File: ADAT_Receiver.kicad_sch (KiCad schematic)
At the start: 21 parts, among them J1 USB_C_Receptacle_PowerOnly_6P, J2 PLR135-T, J3 Conn_01x07_Pin, J4 Conn_01x05_Pin, J5 PLx13xT, SW1 SW_DIP_x03, U1 V1402

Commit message: First order
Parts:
- SW1: footprint Button_Switch_SMD:SW_DIP_SPSTx03_Slide_6.7x9.18mm_W6.73mm_P2.54mm_LowProfile_JPin -> Button_Switch_SMD:SW_DIP_SPSTx03_Slide_6.7x9.18mm_W8.61mm_P2.54mm_LowProfile
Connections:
- net DVCO: now also J4.2 (Pin_2); no longer J4.5 (Pin_5)
- net IO0: now also J4.5 (Pin_5); no longer J4.2 (Pin_2)
- net IO1: now also J4.4 (Pin_4); no longer J4.3 (Pin_3)
- net IO2: now also J4.3 (Pin_3); no longer J4.4 (Pin_4)
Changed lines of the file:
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@@
 	(global_label "DVCO"
 		(shape input)
+		(at 167.64 111.76 180)
+		(fields_autoplaced yes)
+		(effects
+			(font
+				(size 1.27 1.27)
+			)
+			(justify right)
+		)
+		(property "Intersheetrefs" "${INTERSHEET_REFS}"
+			(at 159.6957 111.76 0)
+			(effects
+				(font
+					(size 1.27 1.27)
+				)
+				(justify right)
+				(hide yes)
+			)
+		)
+	)
+	(global_label "IO0"
+		(shape input)
 		(at 167.64 119.38 180)
 		(fields_autoplaced yes)
@@
 		)
 		(property "Intersheetrefs" "${INTERSHEET_REFS}"
-			(at 159.6957 119.38 0)
+			(at 161.51 119.38 0)
+			(effects
+				(font
+					(size 1.27 1.27)
+				)
+				(justify right)
+				(hide yes)
+			)
+		)
+	)
+	(global_label "DVCO"
+		(shape input)
+		(at 149.86 83.82 0)
+		(fields_autoplaced yes)
+		(effects
+			(font
+				(size 1.27 1.27)
+			)
+			(justify left)
+		)
+		(property "Intersheetrefs" "${INTERSHEET_REFS}"
+			(at 157.8043 83.82 0)
+			(effects
+				(font
+					(size 1.27 1.27)
+				)
+				(justify left)
+				(hide yes)
+			)
+		)
+	)
+	(global_label "IO2"
+		(shape input)
+		(at 167.64 114.3 180)
+		(fields_autoplaced yes)
+		(effects
+			(font
+				(size 1.27 1.27)
+			)
+			(justify right)
+		)
+		(property "Intersheetrefs" "${INTERSHEET_REFS}"
+			(at 161.51 114.3 0)
 			(effects
 				(font
@@
 	(global_label "IO0"
 		(shape input)
-		(at 167.64 111.76 180)
+		(at 149.86 73.66 0)
+		(fields_autoplaced yes)
+		(effects
+			(font
+				(size 1.27 1.27)
+			)
+			(justify left)
+		)
+		(property "Intersheetrefs" "${INTERSHEET_REFS}"
+			(at 155.99 73.66 0)
+			(effects
+				(font
+					(size 1.27 1.27)
+				)
+				(justify left)
+				(hide yes)
+			)
+		)
+	)
+	(global_label "IO1"
+		(shape input)
+		(at 167.64 116.84 180)
 		(fields_autoplaced yes)
 		(effects
@@
 		)
 		(property "Intersheetrefs" "${INTERSHEET_REFS}"
-			(at 161.51 111.76 0)
-			(effects
-				(font
-					(size 1.27 1.27)
-				)
-				(justify right)
-				(hide yes)
-			)
-		)
-	)
-	(global_label "DVCO"
-		(shape input)
-		(at 149.86 83.82 0)
-		(fields_autoplaced yes)
-		(effects
-			(font
-				(size 1.27 1.27)
-			)
-			(justify left)
-		)
-		(property "Intersheetrefs" "${INTERSHEET_REFS}"
-			(at 157.8043 83.82 0)
-			(effects
-				(font
-					(size 1.27 1.27)
-				)
-				(justify left)
-				(hide yes)
-			)
-		)
-	)
-	(global_label "IO2"
-		(shape input)
-		(at 167.64 116.84 180)
-		(fields_autoplaced yes)
-		(effects
-			(font
-				(size 1.27 1.27)
-			)
-			(justify right)
-		)
-		(property "Intersheetrefs" "${INTERSHEET_REFS}"
 			(at 161.51 116.84 0)
-			(effects
-				(font
-					(size 1.27 1.27)
-				)
-				(justify right)
-				(hide yes)
-			)
-		)
-	)
-	(global_label "IO0"
-		(shape input)
-		(at 149.86 73.66 0)
-		(fields_autoplaced yes)
-		(effects
-			(font
-				(size 1.27 1.27)
-			)
-			(justify left)
-		)
-		(property "Intersheetrefs" "${INTERSHEET_REFS}"
-			(at 155.99 73.66 0)
-			(effects
-				(font
-					(size 1.27 1.27)
-				)
-				(justify left)
-				(hide yes)
-			)
-		)
-	)
-	(global_label "IO1"
-		(shape input)
-		(at 167.64 114.3 180)
-		(fields_autoplaced yes)
-		(effects
-			(font
-				(size 1.27 1.27)
-			)
-			(justify right)
-		)
-		(property "Intersheetrefs" "${INTERSHEET_REFS}"
-			(at 161.51 114.3 0)
 			(effects
 				(font
@@
 			)
 		)
-		(property "Footprint" "Button_Switch_SMD:SW_DIP_SPSTx03_Slide_6.7x9.18mm_W6.73mm_P2.54mm_LowProfile_JPin"
+		(property "Footprint" "Button_Switch_SMD:SW_DIP_SPSTx03_Slide_6.7x9.18mm_W8.61mm_P2.54mm_LowProfile"
 			(at 73.66 38.1 0)
 			(effects

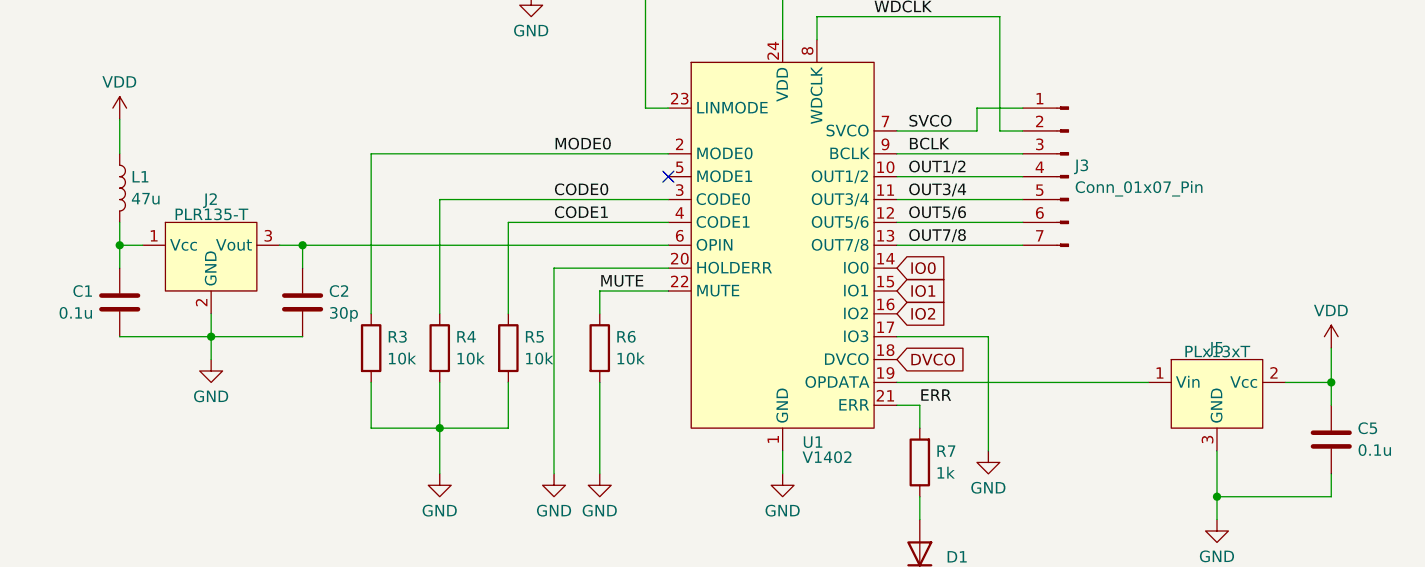
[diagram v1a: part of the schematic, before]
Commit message: Fixed photolink receiver pin assign
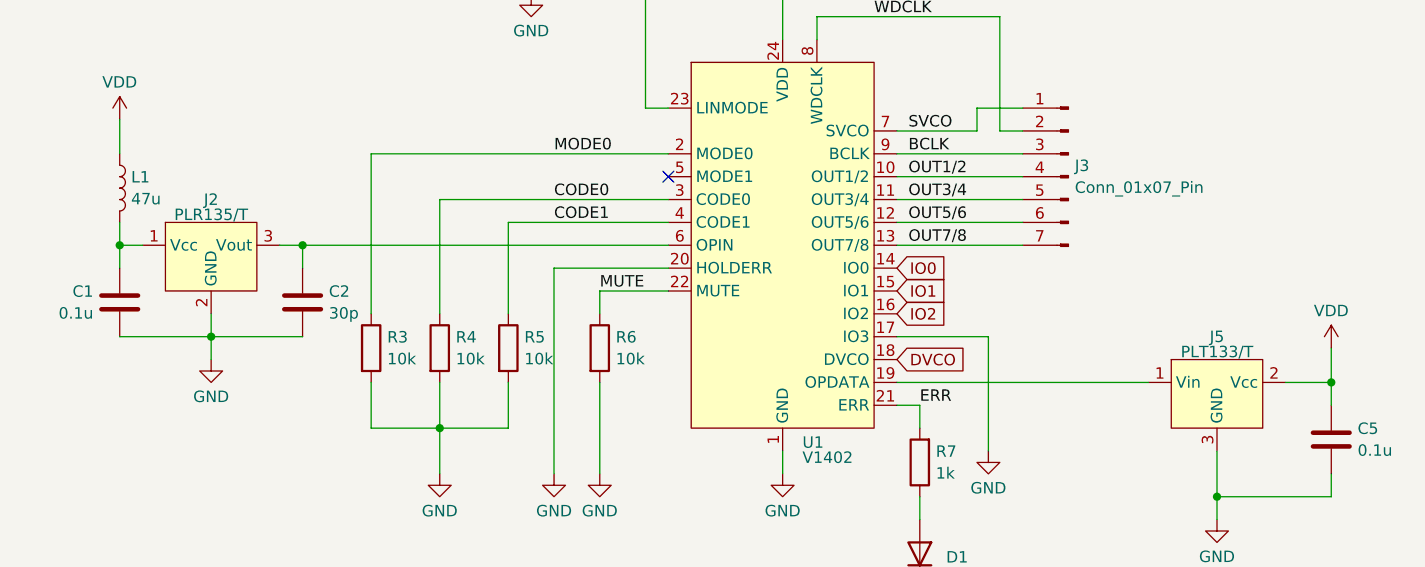
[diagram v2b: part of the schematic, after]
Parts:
- J2: value PLR135-T -> PLR135/T
- J5: value PLx13xT -> PLT133/T
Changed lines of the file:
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@@
+	)
+	(symbol
+		(lib_id "Photolink:PLT133/T")
+		(at 185.42 86.36 0)
+		(unit 1)
+		(exclude_from_sim no)
+		(in_bom yes)
+		(on_board yes)
+		(dnp no)
+		(fields_autoplaced yes)
+		(property "Reference" "J5"
+			(at 185.42 81.2885 0)
+			(effects
+				(font
+					(size 1.27 1.27)
+				)
+			)
+		)
+		(property "Value" "PLT133/T"
+			(at 185.42 82.9699 0)
+			(effects
+				(font
+					(size 1.27 1.27)
+				)
+			)
+		)
+		(property "Footprint" "Photolink:PLx13xT"
+			(at 185.42 86.36 0)
+			(effects
+				(font
+					(size 1.27 1.27)
+				)
+				(hide yes)
+			)
+		)
+		(property "Datasheet" ""
+			(at 185.42 86.36 0)
+			(effects
+				(font
+					(size 1.27 1.27)
+				)
+				(hide yes)
+			)
+		)
+		(property "Description" ""
+			(at 185.42 86.36 0)
+			(effects
+				(font
+					(size 1.27 1.27)
+				)
+				(hide yes)
+			)
+		)
+		(pin "1"
+		)
+		(pin "3"
+		)
+		(pin "2"
+		)
+		(instances
+			(project ""
+				(path "/c71a0874-cde3-4340-9d5d-76a32affaba3"
+					(reference "J5")
+					(unit 1)
+				)
+			)
+		)
 	)
 	(symbol
@@
 			)
 		)
-		(property "Value" "PLR135-T"
+		(property "Value" "PLR135/T"
 			(at 73.66 67.7299 0)
 			(effects
@@
 					(unit 1)
 				)
-			)
-		)
-	)
-	(symbol
-		(lib_id "Photolink:PLT133/T")
-		(at 185.42 86.36 0)
-		(unit 1)
-		(exclude_from_sim no)
-		(in_bom yes)
-		(on_board yes)
-		(dnp no)
-		(property "Reference" "J5"
-			(at 185.42 82.55 0)
-			(effects
-				(font
-					(size 1.27 1.27)
-				)
-			)
-		)
-		(property "Value" "PLx13xT"
-			(at 185.42 82.9699 0)
-			(effects
-				(font
-					(size 1.27 1.27)
-				)
-			)
-		)
-		(property "Footprint" "Photolink:PLx13xT"
-			(at 185.42 86.36 0)
-			(effects
-				(font
-					(size 1.27 1.27)
-				)
-				(hide yes)
-			)
-		)
-		(property "Datasheet" ""
-			(at 185.42 86.36 0)
-			(effects
-				(font
-					(size 1.27 1.27)
-				)
-				(hide yes)
-			)
-		)
-		(property "Description" ""
-			(at 185.42 86.36 0)
-			(effects
-				(font
-					(size 1.27 1.27)
-				)
-				(hide yes)
-			)
-		)
-		(property "LCSC" ""
-			(at 185.42 86.36 0)
-			(effects
-				(font
-					(size 1.27 1.27)
-				)
-				(hide yes)
-			)
-		)
-		(pin "2"
-		)
-		(pin "3"
-		)
-		(pin "1"
-		)
-		(instances
-			(project ""
-				(path "/c71a0874-cde3-4340-9d5d-76a32affaba3"
-					(reference "J5")
-					(unit 1)
-				)
